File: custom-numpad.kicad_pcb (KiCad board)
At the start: 2 copper layers, 25 parts, among them J3 OLED

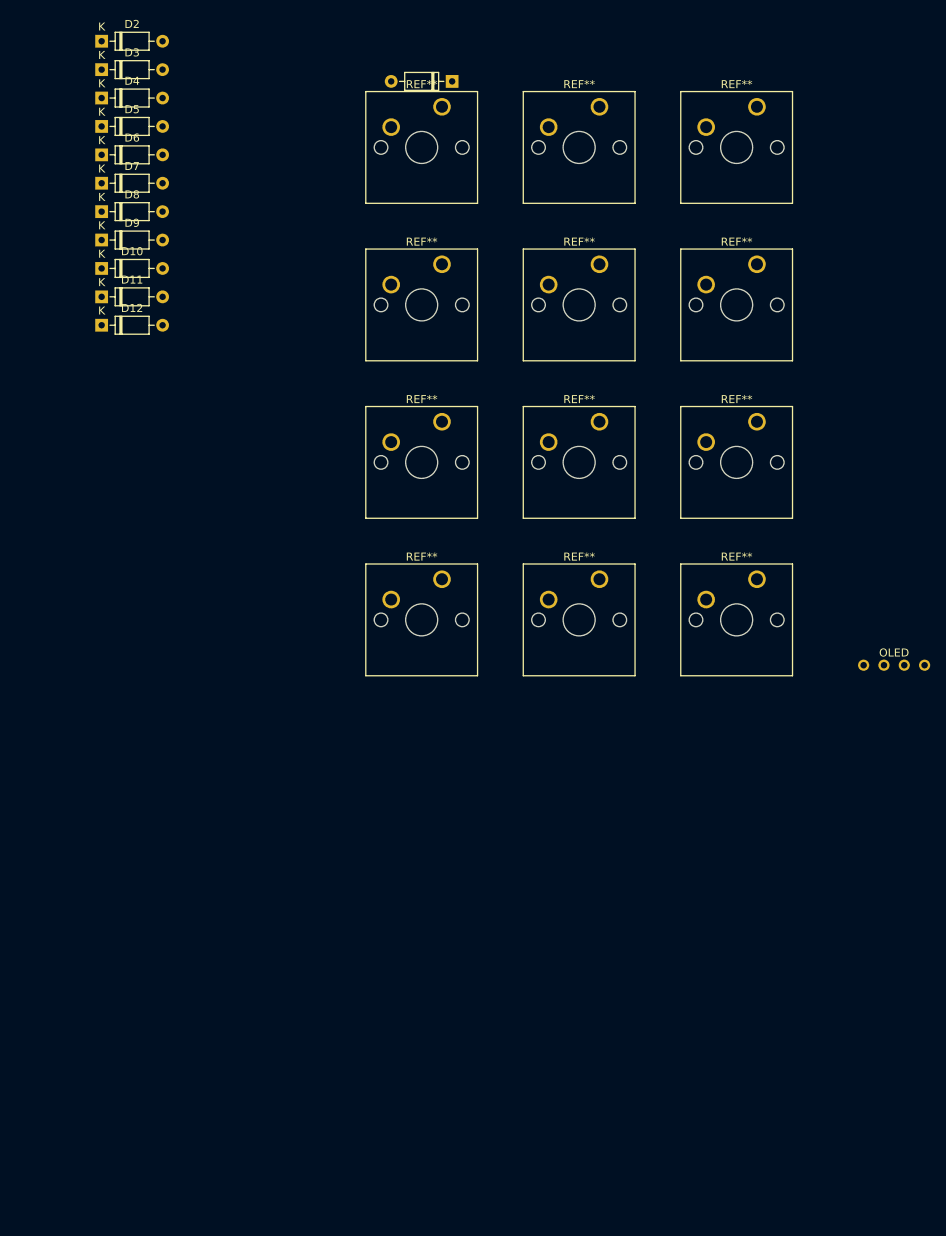
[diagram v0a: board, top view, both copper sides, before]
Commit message: added pad connections and local footprints and schematics
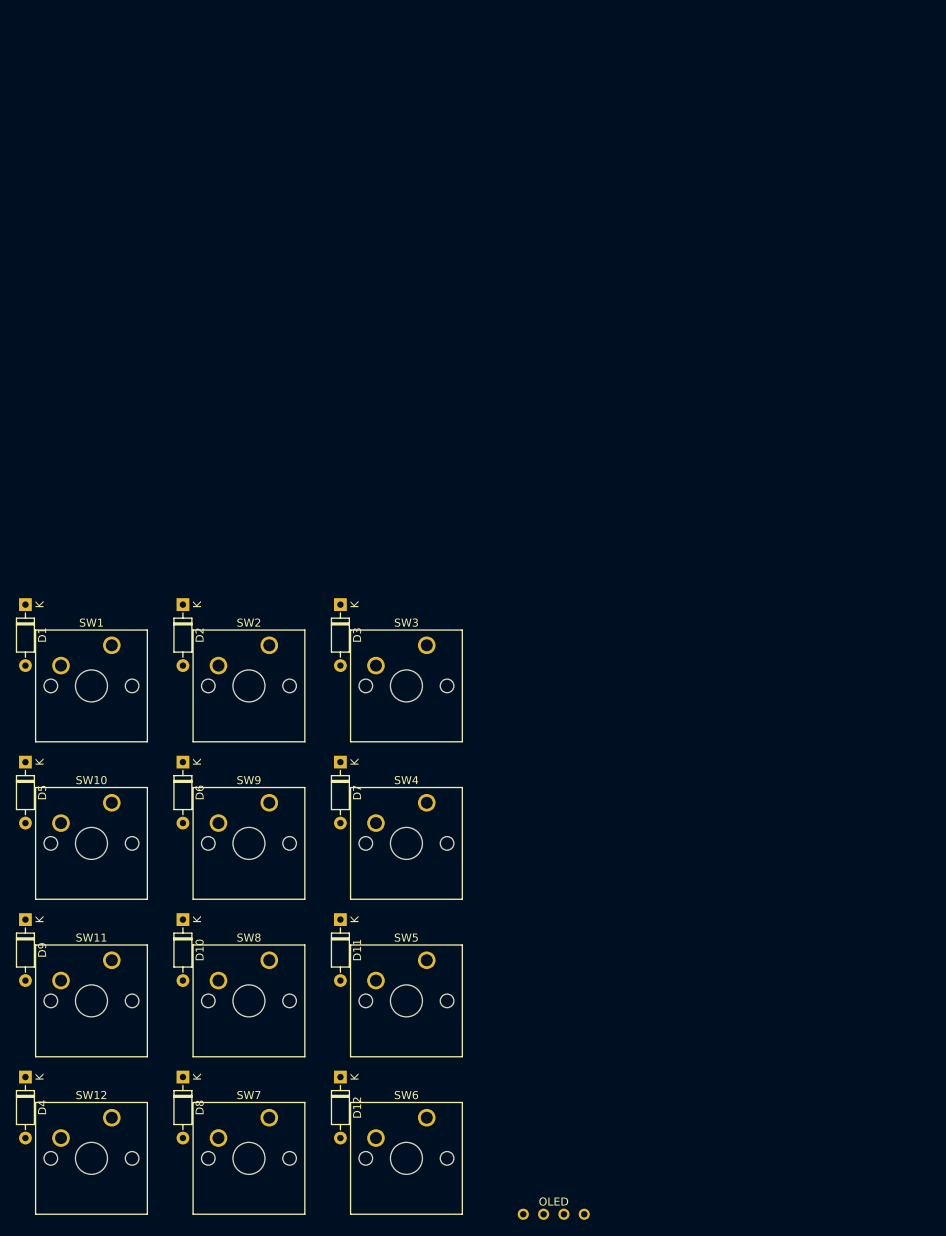
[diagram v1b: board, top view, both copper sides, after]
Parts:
- removed J3: OLED, kbd:OLED_v2
- removed REF** (x12): SW_Cherry_MX_1.00u_PCB, Button_Switch_Keyboard:SW_Cherry_MX_1.00u_PCB
- added Brd1: SSD1306, kbd:OLED_v2, F.Cu at (105.4, 177.8)
- added SW1: SW_Push, Button_Switch_Keyboard:SW_Cherry_MX_1.00u_PCB, F.Cu at (50.2, 106.7)
- added SW10: SW_Push, Button_Switch_Keyboard:SW_Cherry_MX_1.00u_PCB, F.Cu at (50.2, 126.4)
- added SW11: SW_Push, Button_Switch_Keyboard:SW_Cherry_MX_1.00u_PCB, F.Cu at (50.2, 146.1)
- added SW12: SW_Push, Button_Switch_Keyboard:SW_Cherry_MX_1.00u_PCB, F.Cu at (50.2, 165.7)
- added SW2: SW_Push, Button_Switch_Keyboard:SW_Cherry_MX_1.00u_PCB, F.Cu at (69.8, 106.7)
- added SW3: SW_Push, Button_Switch_Keyboard:SW_Cherry_MX_1.00u_PCB, F.Cu at (89.5, 106.7)
- added SW4: SW_Push, Button_Switch_Keyboard:SW_Cherry_MX_1.00u_PCB, F.Cu at (89.5, 126.4)
- added SW5: SW_Push, Button_Switch_Keyboard:SW_Cherry_MX_1.00u_PCB, F.Cu at (89.5, 146.1)
- added SW6: SW_Push, Button_Switch_Keyboard:SW_Cherry_MX_1.00u_PCB, F.Cu at (89.5, 165.7)
- added SW7: SW_Push, Button_Switch_Keyboard:SW_Cherry_MX_1.00u_PCB, F.Cu at (69.8, 165.7)
- added SW8: SW_Push, Button_Switch_Keyboard:SW_Cherry_MX_1.00u_PCB, F.Cu at (69.8, 146.1)
- added SW9: SW_Push, Button_Switch_Keyboard:SW_Cherry_MX_1.00u_PCB, F.Cu at (69.8, 126.4)
- moved D4 122.8 mm to (39.4, 160.7), turned to -90 degrees
- moved D8 108.7 mm to (59.1, 160.7), turned to -90 degrees
- moved D12 98.6 mm to (78.7, 160.7), turned to -90 degrees
- moved D9 85.5 mm to (39.4, 141.0), turned to -90 degrees
- moved D1 84.4 mm to (39.4, 101.6), turned to -90 degrees
- moved D11 83.4 mm to (78.7, 141.0), turned to -90 degrees
- moved D10 82.0 mm to (59.1, 141.0), turned to -90 degrees
- moved D5 80.0 mm to (39.4, 121.3), turned to -90 degrees
- moved D7 78.3 mm to (78.7, 121.3), turned to -90 degrees
- moved D6 76.6 mm to (59.1, 121.3), turned to -90 degrees
- moved D3 73.2 mm to (78.7, 101.6), turned to -90 degrees
- moved D2 71.2 mm to (59.1, 101.6), turned to -90 degrees

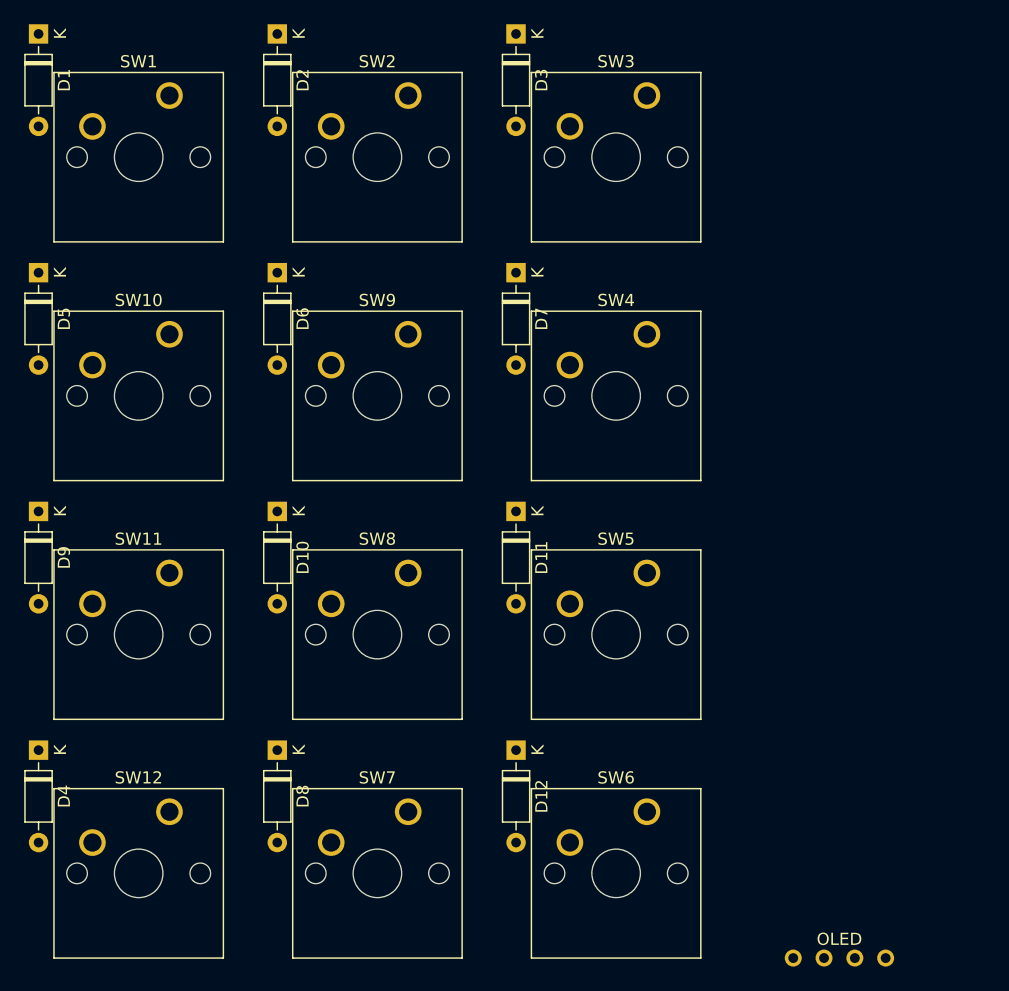
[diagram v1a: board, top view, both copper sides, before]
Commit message: wired up pcb inserted xiao blue print
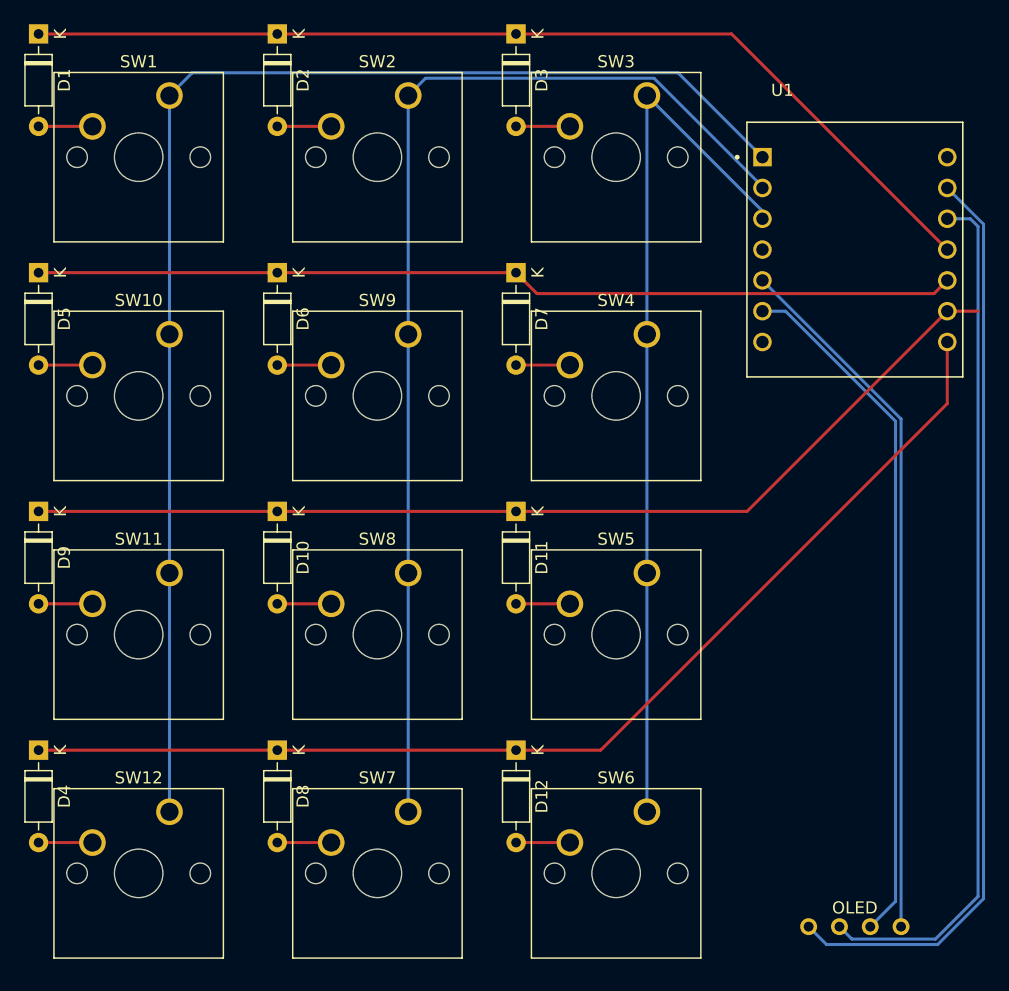
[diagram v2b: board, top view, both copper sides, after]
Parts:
- added U1: SeeeduinoXIAO, seeed xiao:MODULE_102010388, F.Cu at (106.7, 119.4)
- moved Brd1 2.88 mm to (106.7, 175.2)
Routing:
- net C-0: track 0.00 -> 111.6 mm
- net C-1: track 0.00 -> 92.7 mm
- net R-3: track 0.00 -> 91.8 mm
- net R-2: track 0.00 -> 84.3 mm
- net R-0: track 0.00 -> 82.3 mm
- net O-GND: track 0.00 -> 76.4 mm
- net R-1: track 0.00 -> 76.1 mm
- net C-2: track 0.00 -> 73.2 mm
- net O-VCC: track 0.00 -> 71.4 mm
- net O-SDA: track 0.00 -> 58.0 mm
- net O-SCL: track 0.00 -> 57.3 mm
- net Net-(D7-A): track 0.00 -> 4.45 mm
- net Net-(D3-A): track 0.00 -> 4.45 mm
- net Net-(D11-A): track 0.00 -> 4.45 mm
- net Net-(D9-A): track 0.00 -> 4.45 mm
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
